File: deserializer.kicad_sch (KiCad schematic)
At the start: 49 parts, among them U7 MAX96724GTN_VY+, Y1 Resonator_25MHz_ABM8G

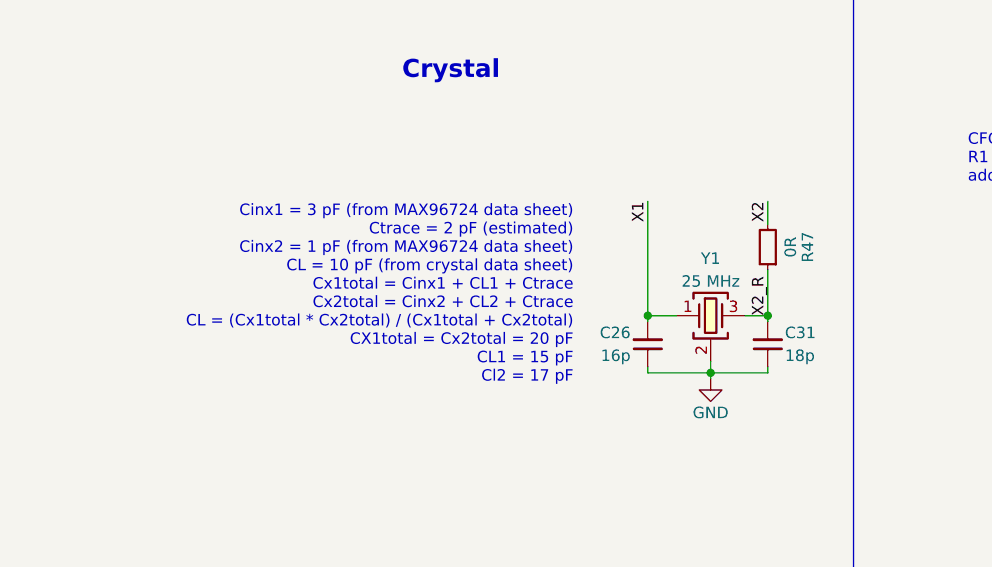
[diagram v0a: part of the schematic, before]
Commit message: Deserializer: update load capacitors and ESD diode symbol
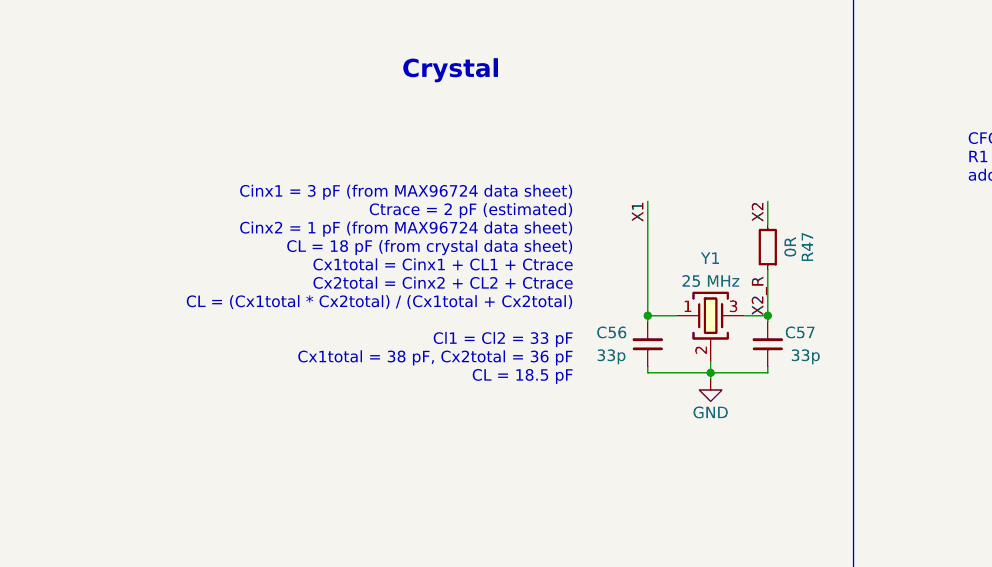
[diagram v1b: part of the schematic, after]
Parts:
- removed C26: C_16p_0402, antmicro-footprints:C_0402_1005Metric, symbol antmicroCapacitors0402:C_16p_0402
- removed C31: C_18p_0402, antmicro-footprints:C_0402_1005Metric, symbol antmicroCapacitors0402:C_18p_0402
- added C56, C57: C_33p_0402, antmicro-footprints:C_0402_1005Metric, symbol antmicroCapacitors0402:C_33p_0402
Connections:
- net GND: now also C56.1, C57.1
- net SIOA_N: now also D4.7
- net SIOA_P: now also D4.6
- net SIOB_N: now also D4.10
- net SIOB_P: now also D4.9
- net SIOC_N: now also D5.7
- net SIOC_P: now also D5.6
- net SIOD_N: now also D5.10
- net SIOD_P: now also D5.9
- net X1: now also C56.2
- net X2_R: now also C57.2
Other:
- note added: "Cinx1 = 3 pF (from MAX96724 data sheet) Ctrace = 2 pF (estimated) Cinx2 = 1 pF (from MAX96724 data sheet) CL = 18 pF (from crystal data sheet) Cx1total = Cinx1 + CL1 + Ctrace Cx2total = Cinx2 + CL2 + Ctrace CL = (Cx1total * Cx2total) / (Cx1total + Cx2total) Cl1 = Cl2 = 33 pF Cx1total = 38 pF, Cx2total = 36 pF CL = 18.5 pF"
- note removed: "Cinx1 = 3 pF (from MAX96724 data sheet) Ctrace = 2 pF (estimated) Cinx2 = 1 pF (from MAX96724 data sheet) CL = 10 pF (from crystal data sheet) Cx1total = Cinx1 + CL1 + Ctrace Cx2total = Cinx2 + CL2 + Ctrace CL = (Cx1total * Cx2total) / (Cx1total + Cx2total) CX1total = Cx2total = 20 pF CL1 = 15 pF Cl2 = 17 pF"
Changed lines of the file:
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@@
     (effects (font (size 1.27 1.27)) (justify left bottom))
   )
-  (text "Cinx1 = 3 pF (from MAX96724 data sheet)\nCtrace = 2 pF (estimated)\nCinx2 = 1 pF (from MAX96724 data sheet)\nCL = 10 pF (from crystal data sheet)\nCx1total = Cinx1 + CL1 + Ctrace\nCx2total = Cinx2 + CL2 + Ctrace\nCL = (Cx1total * Cx2total) / (Cx1total + Cx2total)\nCX1total = Cx2total = 20 pF\nCL1 = 15 pF\nCl2 = 17 pF"
+  (text "Cinx1 = 3 pF (from MAX96724 data sheet)\nCtrace = 2 pF (estimated)\nCinx2 = 1 pF (from MAX96724 data sheet)\nCL = 18 pF (from crystal data sheet)\nCx1total = Cinx1 + CL1 + Ctrace\nCx2total = Cinx2 + CL2 + Ctrace\nCL = (Cx1total * Cx2total) / (Cx1total + Cx2total)\n\nCl1 = Cl2 = 33 pF\nCx1total = 38 pF, Cx2total = 36 pF\nCL = 18.5 pF"
     (at 69.215 260.985 180)
     (effects (font (size 1.27 1.27)) (justify right bottom))
@@
     (pin "1")
   )
+  (symbol (lib_id "antmicroCapacitors0402:C_33p_0402") (at 77.47 259.08 90) (unit 1)
+    (in_bom yes) (on_board yes)
+    (property "Reference" "C56" (id 0) (at 71.755 255.27 90)
+      (effects (font (size 1.27 1.27) (thickness 0.15)) (justify right))
+    )
+    (property "Value" "C_33p_0402" (id 1) (at 87.63 238.76 0)
+      (effects (font (size 1.27 1.27) (thickness 0.15)) (justify left bottom) hide)
+    )
+    (property "Footprint" "antmicro-footprints:C_0402_1005Metric" (id 2) (at 90.17 238.76 0)
+      (effects (font (size 1.27 1.27) (thickness 0.15)) (justify left bottom) hide)
+    )
+    (property "Datasheet" "https://spicat.kyocera-avx.com/product/mlcc/chartview/04025A330FAT2A/" (id 3) (at 92.71 238.76 0)
+      (effects (font (size 1.27 1.27) (thickness 0.15)) (justify left bottom) hide)
+    )
+    (property "MPN" "04025A330FAT2A" (id 4) (at 95.25 238.76 0)
+      (effects (font (size 1.27 1.27) (thickness 0.15)) (justify left bottom) hide)
+    )
+    (property "Manufacturer" "KYOCERA AVX" (id 5) (at 97.79 238.76 0)
+      (effects (font (size 1.27 1.27) (thickness 0.15)) (justify left bottom) hide)
+    )
+    (property "License" "Apache-2.0" (id 6) (at 100.33 238.76 0)
+      (effects (font (size 1.27 1.27) (thickness 0.15)) (justify left bottom) hide)
+    )
+    (property "Author" "Antmicro" (id 7) (at 102.87 238.76 0)
+      (effects (font (size 1.27 1.27) (thickness 0.15)) (justify left bottom) hide)
+    )
+    (property "Val" "33p" (id 8) (at 71.755 257.81 90)
+      (effects (font (size 1.27 1.27) (thickness 0.15)) (justify right))
+    )
+    (property "Voltage" "" (id 9) (at 105.41 238.76 0)
+      (effects (font (size 1.27 1.27)) (justify left bottom) hide)
+    )
+    (property "Dielectric" "" (id 10) (at 107.95 238.76 0)
+      (effects (font (size 1.27 1.27)) (justify left bottom) hide)
+    )
+    (pin "1")
+    (pin "2")
+  )
   (symbol (lib_id "antmicropower:+1V8") (at 214.63 88.9 0) (unit 1)
     (in_bom yes) (on_board yes)
@@
     (property "Current" "1A" (id 10) (at 400.685 96.52 0)
       (effects (font (size 1.27 1.27) (thickness 0.15)) (justify left bottom) hide)
-    )
-    (pin "1")
-    (pin "2")
-  )
-  (symbol (lib_id "antmicroCapacitors0402:C_16p_0402") (at 77.47 259.08 270) (mirror x) (unit 1)
-    (in_bom yes) (on_board yes)
-    (property "Reference" "C26" (id 0) (at 75.565 255.27 90)
-      (effects (font (size 1.27 1.27) (thickness 0.15)) (justify right))
-    )
-    (property "Value" "C_16p_0402" (id 1) (at 67.31 238.76 0)
-      (effects (font (size 1.27 1.27) (thickness 0.15)) (justify left bottom) hide)
-    )
-    (property "Footprint" "antmicro-footprints:C_0402_1005Metric" (id 2) (at 64.77 238.76 0)
-      (effects (font (size 1.27 1.27) (thickness 0.15)) (justify left bottom) hide)
-    )
-    (property "Datasheet" "https://www.passivecomponent.com/wp-content/uploads/datasheet/WTC_MLCC_General_Purpose.pdf" (id 3) (at 62.23 238.76 0)
-      (effects (font (size 1.27 1.27) (thickness 0.15)) (justify left bottom) hide)
-    )
-    (property "MPN" "0402N160J500CT" (id 4) (at 59.69 238.76 0)
-      (effects (font (size 1.27 1.27) (thickness 0.15)) (justify left bottom) hide)
-    )
-    (property "Manufacturer" "Walsin" (id 5) (at 57.15 238.76 0)
-      (effects (font (size 1.27 1.27) (thickness 0.15)) (justify left bottom) hide)
-    )
-    (property "License" "Apache-2.0" (id 6) (at 54.61 238.76 0)
-      (effects (font (size 1.27 1.27) (thickness 0.15)) (justify left bottom) hide)
-    )
-    (property "Author" "Antmicro" (id 7) (at 52.07 238.76 0)
-      (effects (font (size 1.27 1.27) (thickness 0.15)) (justify left bottom) hide)
-    )
-    (property "Val" "16p" (id 8) (at 75.565 257.81 90)
-      (effects (font (size 1.27 1.27) (thickness 0.15)) (justify right))
-    )
-    (property "Voltage" "" (id 9) (at 49.53 238.76 0)
-      (effects (font (size 1.27 1.27)) (justify left bottom) hide)
-    )
-    (property "Dielectric" "" (id 10) (at 46.99 238.76 0)
-      (effects (font (size 1.27 1.27)) (justify left bottom) hide)
     )
     (pin "1")
@@
     )
     (property "Dielectric" "X5R" (id 10) (at 71.12 147.32 0)
-      (effects (font (size 1.27 1.27)) (justify left bottom) hide)
-    )
-    (pin "1")
-    (pin "2")
-  )
-  (symbol (lib_id "antmicroCapacitors0402:C_18p_0402") (at 90.805 259.08 90) (unit 1)
-    (in_bom yes) (on_board yes)
-    (property "Reference" "C31" (id 0) (at 92.71 255.27 90)
-      (effects (font (size 1.27 1.27) (thickness 0.15)) (justify right))
-    )
-    (property "Value" "C_18p_0402" (id 1) (at 100.965 238.76 0)
-      (effects (font (size 1.27 1.27) (thickness 0.15)) (justify left bottom) hide)
-    )
-    (property "Footprint" "antmicro-footprints:C_0402_1005Metric" (id 2) (at 103.505 238.76 0)
-      (effects (font (size 1.27 1.27) (thickness 0.15)) (justify left bottom) hide)
-    )
-    (property "Datasheet" "https://product.samsungsem.com/mlcc/CL05C180JB51PN.do" (id 3) (at 106.045 238.76 0)
-      (effects (font (size 1.27 1.27) (thickness 0.15)) (justify left bottom) hide)
-    )
-    (property "MPN" "CL05C180JB51PNC" (id 4) (at 108.585 238.76 0)
-      (effects (font (size 1.27 1.27) (thickness 0.15)) (justify left bottom) hide)
-    )
-    (property "Manufacturer" "Samsung Electro-Mechanics" (id 5) (at 111.125 238.76 0)
-      (effects (font (size 1.27 1.27) (thickness 0.15)) (justify left bottom) hide)
-    )
-    (property "License" "Apache-2.0" (id 6) (at 113.665 238.76 0)
-      (effects (font (size 1.27 1.27) (thickness 0.15)) (justify left bottom) hide)
-    )
-    (property "Author" "Antmicro" (id 7) (at 116.205 238.76 0)
-      (effects (font (size 1.27 1.27) (thickness 0.15)) (justify left bottom) hide)
-    )
-    (property "Val" "18p" (id 8) (at 92.71 257.81 90)
-      (effects (font (size 1.27 1.27) (thickness 0.15)) (justify right))
-    )
-    (property "Voltage" "" (id 9) (at 118.745 238.76 0)
-      (effects (font (size 1.27 1.27)) (justify left bottom) hide)
-    )
-    (property "Dielectric" "" (id 10) (at 121.285 238.76 0)
       (effects (font (size 1.27 1.27)) (justify left bottom) hide)
     )
@@
     (pin "8")
     (pin "9")
+  )
+  (symbol (lib_id "antmicroCapacitors0402:C_33p_0402") (at 90.805 259.08 90) (unit 1)
+    (in_bom yes) (on_board yes)
+    (property "Reference" "C57" (id 0) (at 92.71 255.27 90)
+      (effects (font (size 1.27 1.27) (thickness 0.15)) (justify right))
+    )
+    (property "Value" "C_33p_0402" (id 1) (at 100.965 238.76 0)
+      (effects (font (size 1.27 1.27) (thickness 0.15)) (justify left bottom) hide)
+    )
+    (property "Footprint" "antmicro-footprints:C_0402_1005Metric" (id 2) (at 103.505 238.76 0)
+      (effects (font (size 1.27 1.27) (thickness 0.15)) (justify left bottom) hide)
+    )
+    (property "Datasheet" "https://spicat.kyocera-avx.com/product/mlcc/chartview/04025A330FAT2A/" (id 3) (at 106.045 238.76 0)
+      (effects (font (size 1.27 1.27) (thickness 0.15)) (justify left bottom) hide)
+    )
+    (property "MPN" "04025A330FAT2A" (id 4) (at 108.585 238.76 0)
+      (effects (font (size 1.27 1.27) (thickness 0.15)) (justify left bottom) hide)
+    )
+    (property "Manufacturer" "KYOCERA AVX" (id 5) (at 111.125 238.76 0)
+      (effects (font (size 1.27 1.27) (thickness 0.15)) (justify left bottom) hide)
+    )
+    (property "License" "Apache-2.0" (id 6) (at 113.665 238.76 0)
+      (effects (font (size 1.27 1.27) (thickness 0.15)) (justify left bottom) hide)
+    )
+    (property "Author" "Antmicro" (id 7) (at 116.205 238.76 0)
+      (effects (font (size 1.27 1.27) (thickness 0.15)) (justify left bottom) hide)
+    )
+    (property "Val" "33p" (id 8) (at 93.345 257.81 90)
+      (effects (font (size 1.27 1.27) (thickness 0.15)) (justify right))
+    )
+    (property "Voltage" "" (id 9) (at 118.745 238.76 0)
+      (effects (font (size 1.27 1.27)) (justify left bottom) hide)
+    )
+    (property "Dielectric" "" (id 10) (at 121.285 238.76 0)
+      (effects (font (size 1.27 1.27)) (justify left bottom) hide)
+    )
+    (pin "1")
+    (pin "2")
   )
   (symbol (lib_id "antmicroInterfaceControllers:MAX96724GTN_VY+") (at 280.67 113.03 0) (unit 1)
@@
     (pin "2")
   )
-  (symbol (lib_id "antmicroTVSDiodes:PESD4USB5U-TTS") (at 126.365 197.485 270) (unit 1)
+  (symbol (lib_name "PESD4USB5U-TTS_1") (lib_id "antmicroTVSDiodes:PESD4USB5U-TTS") (at 126.365 197.485 270) (unit 1)
     (in_bom yes) (on_board yes)
     (property "Reference" "D5" (id 0) (at 114.935 206.375 90)

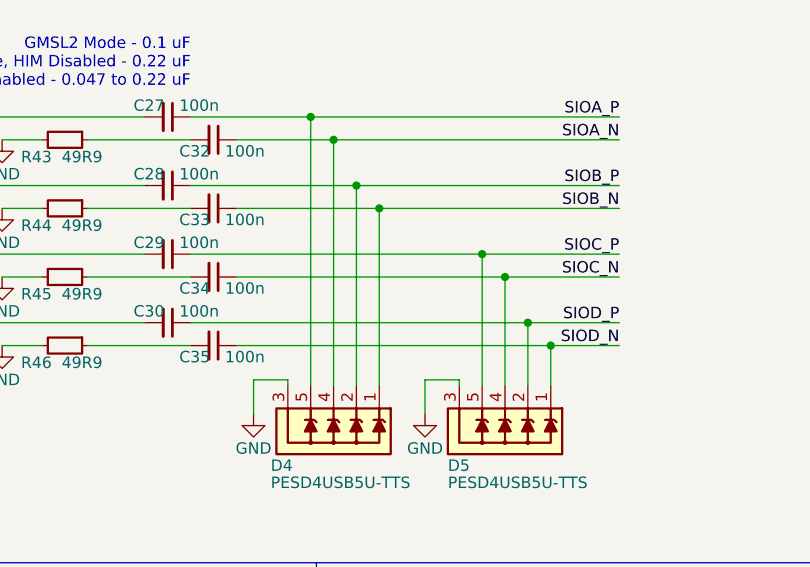
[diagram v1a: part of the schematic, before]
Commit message: Power: add boost converter labels
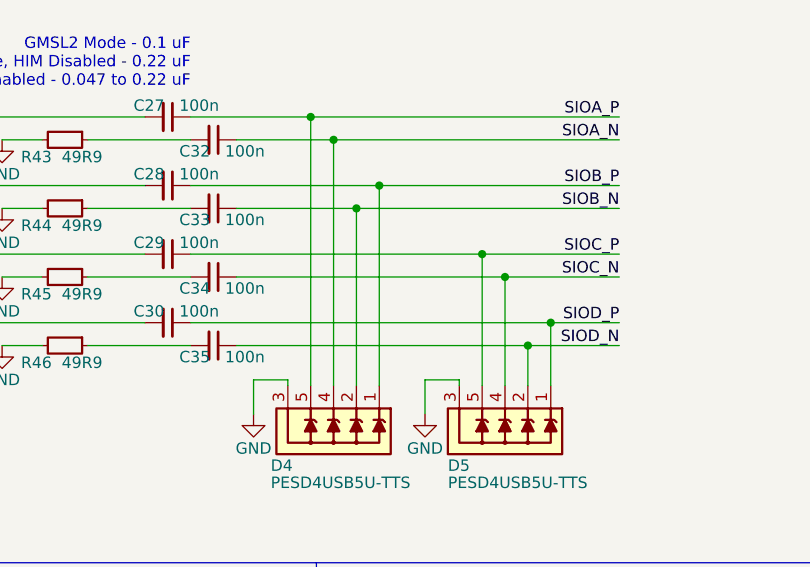
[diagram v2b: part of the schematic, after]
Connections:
- net SIOB_N: now also D4.2, D4.9; no longer D4.1, D4.10
- net SIOB_P: now also D4.1, D4.10; no longer D4.2, D4.9
- net SIOD_N: now also D5.2, D5.9; no longer D5.1, D5.10
- net SIOD_P: now also D5.1, D5.10; no longer D5.2, D5.9
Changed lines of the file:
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@@
   (junction (at 102.235 170.18) (diameter 0) (color 0 0 0 0)
   )
+  (junction (at 126.365 190.5) (diameter 0) (color 0 0 0 0)
+  )
   (junction (at 242.57 96.52) (diameter 0) (color 0 0 0 0)
   )
@@
   (junction (at 242.57 115.57) (diameter 0) (color 0 0 0 0)
   )
-  (junction (at 126.365 193.04) (diameter 0) (color 0 0 0 0)
-  )
   (junction (at 342.265 118.11) (diameter 0) (color 0 0 0 0)
   )
@@
   (junction (at 252.73 194.31) (diameter 0) (color 0 0 0 0)
   )
+  (junction (at 107.315 175.26) (diameter 0) (color 0 0 0 0)
+  )
   (junction (at 90.805 253.365) (diameter 0) (color 0 0 0 0)
   )
@@
   (junction (at 118.745 182.88) (diameter 0) (color 0 0 0 0)
   )
-  (junction (at 107.315 177.8) (diameter 0) (color 0 0 0 0)
-  )
-  (junction (at 104.775 175.26) (diameter 0) (color 0 0 0 0)
-  )
   (junction (at 243.84 194.31) (diameter 0) (color 0 0 0 0)
   )
@@
   (junction (at 84.455 259.715) (diameter 0) (color 0 0 0 0)
   )
+  (junction (at 104.775 177.8) (diameter 0) (color 0 0 0 0)
+  )
   (junction (at 232.41 115.57) (diameter 0) (color 0 0 0 0)
   )
+  (junction (at 123.825 193.04) (diameter 0) (color 0 0 0 0)
+  )
   (junction (at 235.585 194.31) (diameter 0) (color 0 0 0 0)
-  )
-  (junction (at 123.825 190.5) (diameter 0) (color 0 0 0 0)
   )
   (no_connect (at 316.23 133.35))
@@
     (stroke (width 0) (type default) (color 0 0 0 0))
   )
+  (wire (pts (xy 126.365 190.5) (xy 133.985 190.5))
+    (stroke (width 0) (type default) (color 0 0 0 0))
+  )
   (wire (pts (xy 316.23 153.67) (xy 329.565 153.67))
     (stroke (width 0) (type default) (color 0 0 0 0))
@@
     (stroke (width 0) (type default) (color 0 0 0 0))
   )
-  (wire (pts (xy 123.825 190.5) (xy 123.825 197.485))
-    (stroke (width 0) (type default) (color 0 0 0 0))
-  )
   (wire (pts (xy 271.145 148.59) (xy 280.67 148.59))
     (stroke (width 0) (type default) (color 0 0 0 0))
@@
     (stroke (width 0) (type default) (color 0 0 0 0))
   )
-  (wire (pts (xy 107.315 177.8) (xy 133.985 177.8))
+  (wire (pts (xy 91.44 177.8) (xy 104.775 177.8))
     (stroke (width 0) (type default) (color 0 0 0 0))
   )
@@
     (stroke (width 0) (type default) (color 0 0 0 0))
   )
-  (wire (pts (xy 91.44 193.04) (xy 126.365 193.04))
-    (stroke (width 0) (type default) (color 0 0 0 0))
-  )
-  (wire (pts (xy 123.825 190.5) (xy 133.985 190.5))
+  (wire (pts (xy 86.36 190.5) (xy 126.365 190.5))
     (stroke (width 0) (type default) (color 0 0 0 0))
   )
@@
     (stroke (width 0) (type default) (color 0 0 0 0))
   )
-  (wire (pts (xy 91.44 177.8) (xy 107.315 177.8))
-    (stroke (width 0) (type default) (color 0 0 0 0))
-  )
   (bus (pts (xy 271.145 162.56) (xy 271.145 165.1))
     (stroke (width 0) (type default) (color 0 0 0 0))
@@
     (stroke (width 0) (type default) (color 0 0 0 0))
   )
-  (wire (pts (xy 104.775 175.26) (xy 104.775 197.485))
-    (stroke (width 0) (type default) (color 0 0 0 0))
-  )
   (wire (pts (xy 214.63 115.57) (xy 214.63 114.3))
     (stroke (width 0) (type default) (color 0 0 0 0))
@@
     (stroke (width 0) (type default) (color 0 0 0 0))
   )
+  (wire (pts (xy 107.315 175.26) (xy 133.985 175.26))
+    (stroke (width 0) (type default) (color 0 0 0 0))
+  )
   (wire (pts (xy 277.495 186.69) (xy 280.67 186.69))
     (stroke (width 0) (type default) (color 0 0 0 0))
@@
     (stroke (width 0) (type default) (color 0 0 0 0))
   )
-  (wire (pts (xy 126.365 193.04) (xy 126.365 197.485))
-    (stroke (width 0) (type default) (color 0 0 0 0))
-  )
   (bus (pts (xy 332.105 165.1) (xy 337.82 165.1))
     (stroke (width 0) (type default) (color 0 0 0 0))
@@
     (stroke (width 0) (type default) (color 0 0 0 0))
   )
+  (wire (pts (xy 123.825 193.04) (xy 123.825 197.485))
+    (stroke (width 0) (type default) (color 0 0 0 0))
+  )
   (wire (pts (xy 271.145 96.52) (xy 271.145 113.03))
     (stroke (width 0) (type default) (color 0 0 0 0))
@@
     (stroke (width 0) (type default) (color 0 0 0 0))
   )
+  (wire (pts (xy 123.825 193.04) (xy 133.985 193.04))
+    (stroke (width 0) (type default) (color 0 0 0 0))
+  )
   (wire (pts (xy 326.39 105.41) (xy 326.39 96.52))
     (stroke (width 0) (type default) (color 0 0 0 0))
@@
     (stroke (width 0) (type default) (color 0 0 0 0))
   )
-  (wire (pts (xy 107.315 177.8) (xy 107.315 197.485))
-    (stroke (width 0) (type default) (color 0 0 0 0))
-  )
   (wire (pts (xy 62.865 182.88) (xy 81.28 182.88))
     (stroke (width 0) (type default) (color 0 0 0 0))
@@
     (stroke (width 0) (type default) (color 0 0 0 0))
   )
-  (wire (pts (xy 126.365 193.04) (xy 133.985 193.04))
+  (wire (pts (xy 91.44 193.04) (xy 123.825 193.04))
+    (stroke (width 0) (type default) (color 0 0 0 0))
+  )
+  (wire (pts (xy 104.775 177.8) (xy 104.775 197.485))
     (stroke (width 0) (type default) (color 0 0 0 0))
   )
@@
     (stroke (width 0) (type default) (color 0 0 0 0))
   )
-  (wire (pts (xy 86.36 175.26) (xy 104.775 175.26))
+  (wire (pts (xy 86.36 175.26) (xy 107.315 175.26))
     (stroke (width 0) (type default) (color 0 0 0 0))
   )
@@
     (stroke (width 0) (type default) (color 0 0 0 0))
   )
+  (wire (pts (xy 126.365 190.5) (xy 126.365 197.485))
+    (stroke (width 0) (type default) (color 0 0 0 0))
+  )
   (wire (pts (xy 251.46 122.555) (xy 251.46 121.92))
     (stroke (width 0) (type default) (color 0 0 0 0))
@@
     (stroke (width 0) (type default) (color 0 0 0 0))
   )
+  (wire (pts (xy 104.775 177.8) (xy 133.985 177.8))
+    (stroke (width 0) (type default) (color 0 0 0 0))
+  )
   (wire (pts (xy 242.57 115.57) (xy 251.46 115.57))
     (stroke (width 0) (type default) (color 0 0 0 0))
@@
     (stroke (width 0) (type default) (color 0 0 0 0))
   )
-  (wire (pts (xy 86.36 190.5) (xy 123.825 190.5))
-    (stroke (width 0) (type default) (color 0 0 0 0))
-  )
   (wire (pts (xy 271.145 140.97) (xy 280.67 140.97))
     (stroke (width 0) (type default) (color 0 0 0 0))
@@
     (stroke (width 0) (type default) (color 0 0 0 0))
   )
+  (wire (pts (xy 107.315 175.26) (xy 107.315 197.485))
+    (stroke (width 0) (type default) (color 0 0 0 0))
+  )
   (wire (pts (xy 65.405 185.42) (xy 69.85 185.42))
     (stroke (width 0) (type default) (color 0 0 0 0))
@@
     (stroke (width 0) (type default) (color 0 0 0 0))
   )
-  (wire (pts (xy 104.775 175.26) (xy 133.985 175.26))
-    (stroke (width 0) (type default) (color 0 0 0 0))
-  )
